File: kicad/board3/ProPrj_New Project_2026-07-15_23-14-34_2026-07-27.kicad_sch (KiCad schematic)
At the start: 141 parts, among them P1 WJ500V-5.08-2P, P2 WJ500V-5.08-2P, Q1 AO4406A, Q2 AO4406A, SW1 HX TS4538CJ 250gf 009, SW2 HX TS4538CJ 250gf 009, SW3 HX TS4538CJ 250gf 009, SW4 HX TS4538CJ 250gf 009, SW6 HX TS4538CJ 250gf 009, SW7 HX TS4538CJ 250gf 009, U1 STM32H755ZIT6, U10 TBD62083AFWG, U2 W25Q512JVEIQ TR, U3 TPS563201DDCR, U4 CH224K, U5 LM74700QDBVRQ1, U6 LM74700QDBVRQ1, U7 FM24CL64B-GTR, U8 TJA1051T/3/1J, U9 TJA1051T/3/1J, X1 25MHz

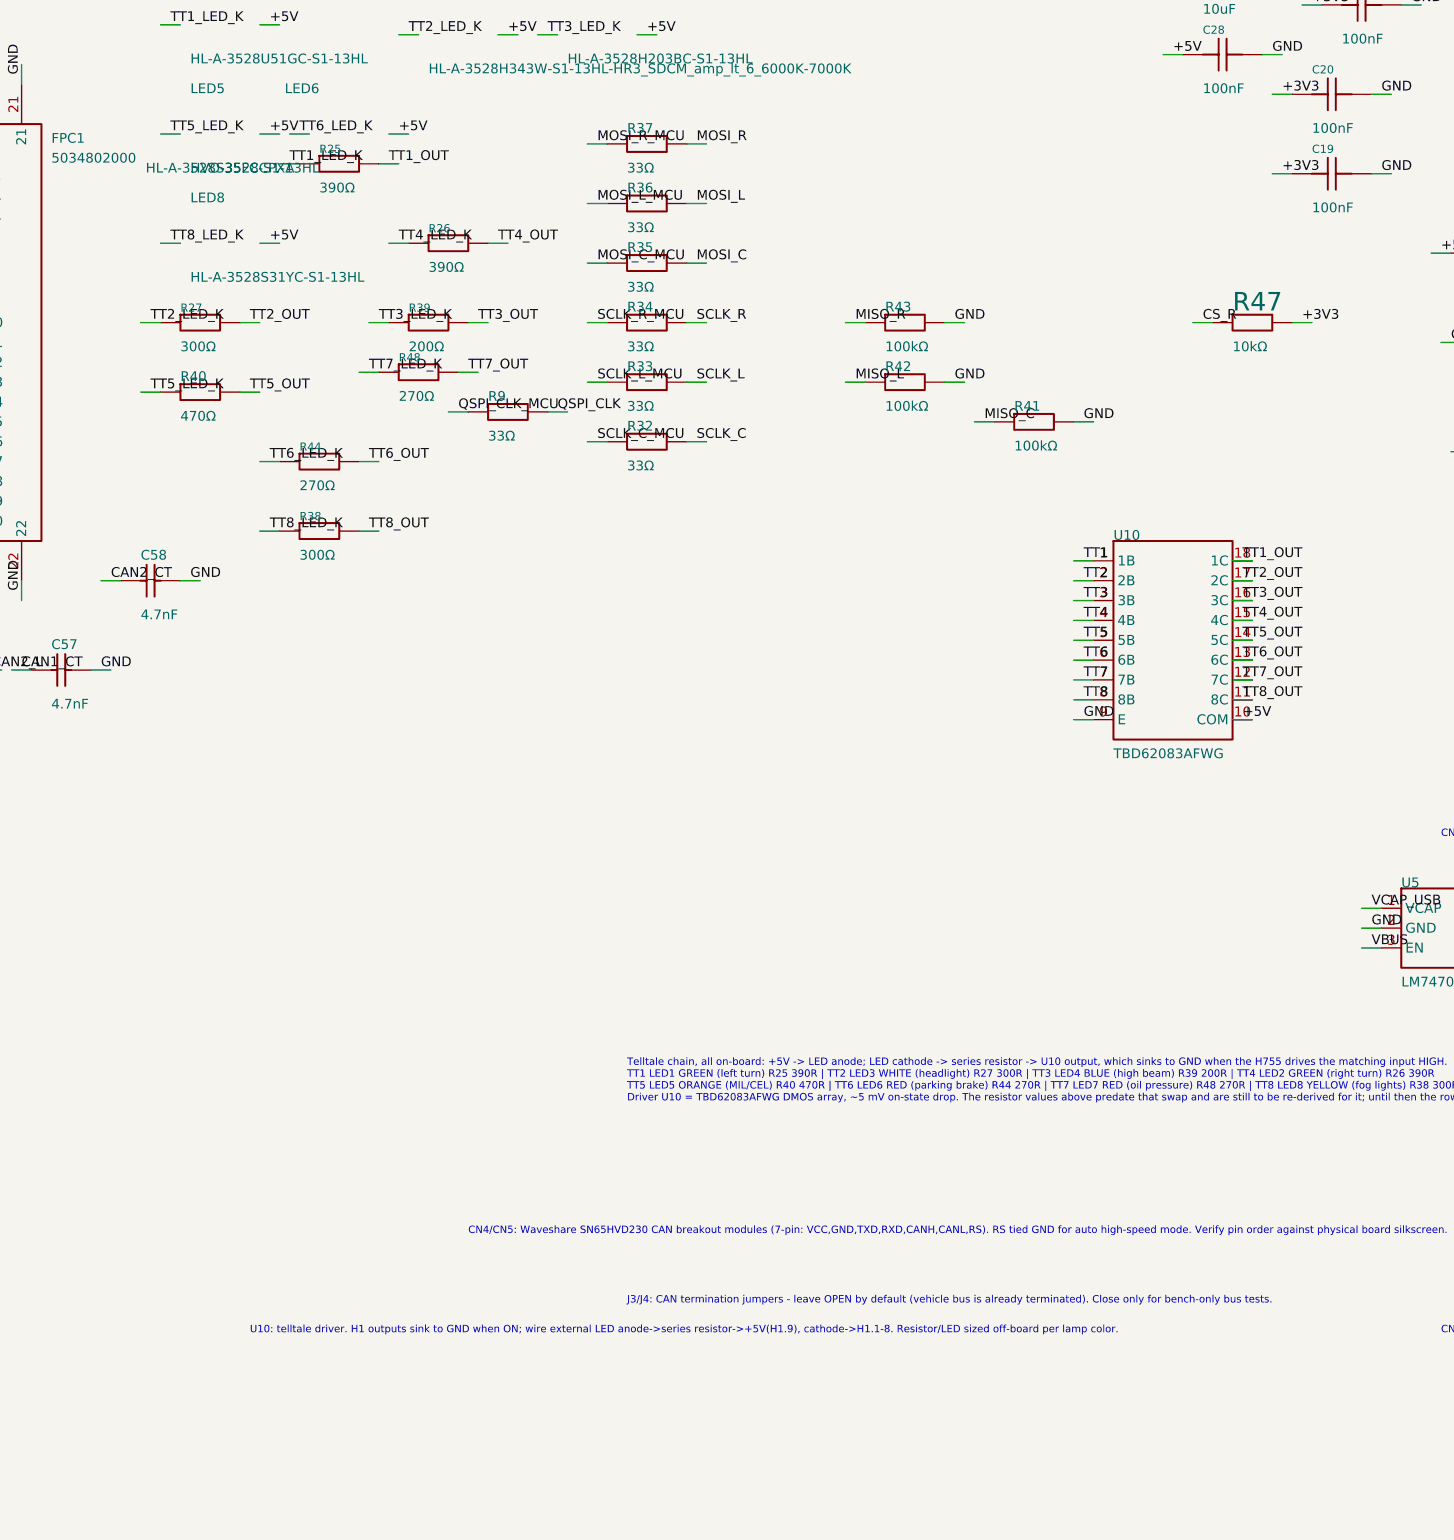
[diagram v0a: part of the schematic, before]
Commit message: feat(kicad): U19 - schematic moves telltale drive onto two AW9523B expanders
Datasheet gate PASSED before any wiring (AW9523B V2.4, official Awinic PDF):
IMAX 31.9/37/43.1 mA with 256 linear steps (10-20 mA targets sit mid-range;
GCR ISEL can halve the range for double resolution); all pins rated -0.3..6 V
independent of VCC; I2C thresholds FIXED at VIH 1.4 V / VIL 0.4 V, so the
3.3 V-pulled trunk works at any VCC; POR defaults are GPIO *output* with the
state set by the AD straps - GND/GND would light every LED at power-up.

Decisions locked by the gate: VCC = +5 V both ICs (POR high equals the
anode rail, LEDs hard off; 3.3 V would leave ~1.7 V across red/yellow).
West U11 = AD1/AD0 both +5V -> 0x5B, every port POR-safe. East U12 =
AD1 +5V / AD0 GND -> 0x5A, LEDs on its POR-safe P1_4-P1_7 (west matches for
firmware symmetry). RSTN tied to +5V (internal 100k pull-DOWN would hold the
chip in reset). INTN + 24 spare I/O carry no_connects.

Schematic: U10 (TBD62083) and R25-R27/R38-R40/R44/R48 deleted with their
TT/TT_OUT labels and wires; C61/C62 100nF (C14663) decouple the new ICs.
Netlist diff is exactly the intended topology: 16 TT nets gone, each
TTn_LED_K keeps its LED and gains its expander pin, I2C gains two loads,
BTN nets byte-identical (KTD20/R40 proof). ERC 171 -> 155 (pin_not_driven
71 -> 55), no new types. All surviving instances verified byte-identical.

Board deliberately NOT yet synced - not fab-ready at this boundary. Next:
Kevin runs Update PCB from Schematic (KiCad restarted, re-link by reference)
per KTD12, then U20 places and routes.

Known pre-existing, not introduced here: kicad_lcsc duplicates flags 10k
R0603 dual-sourced (C25804 x4 / C98220 x6) on parts this change never touched.

Co-Authored-By: Claude Fable 5 <noreply@anthropic.com>
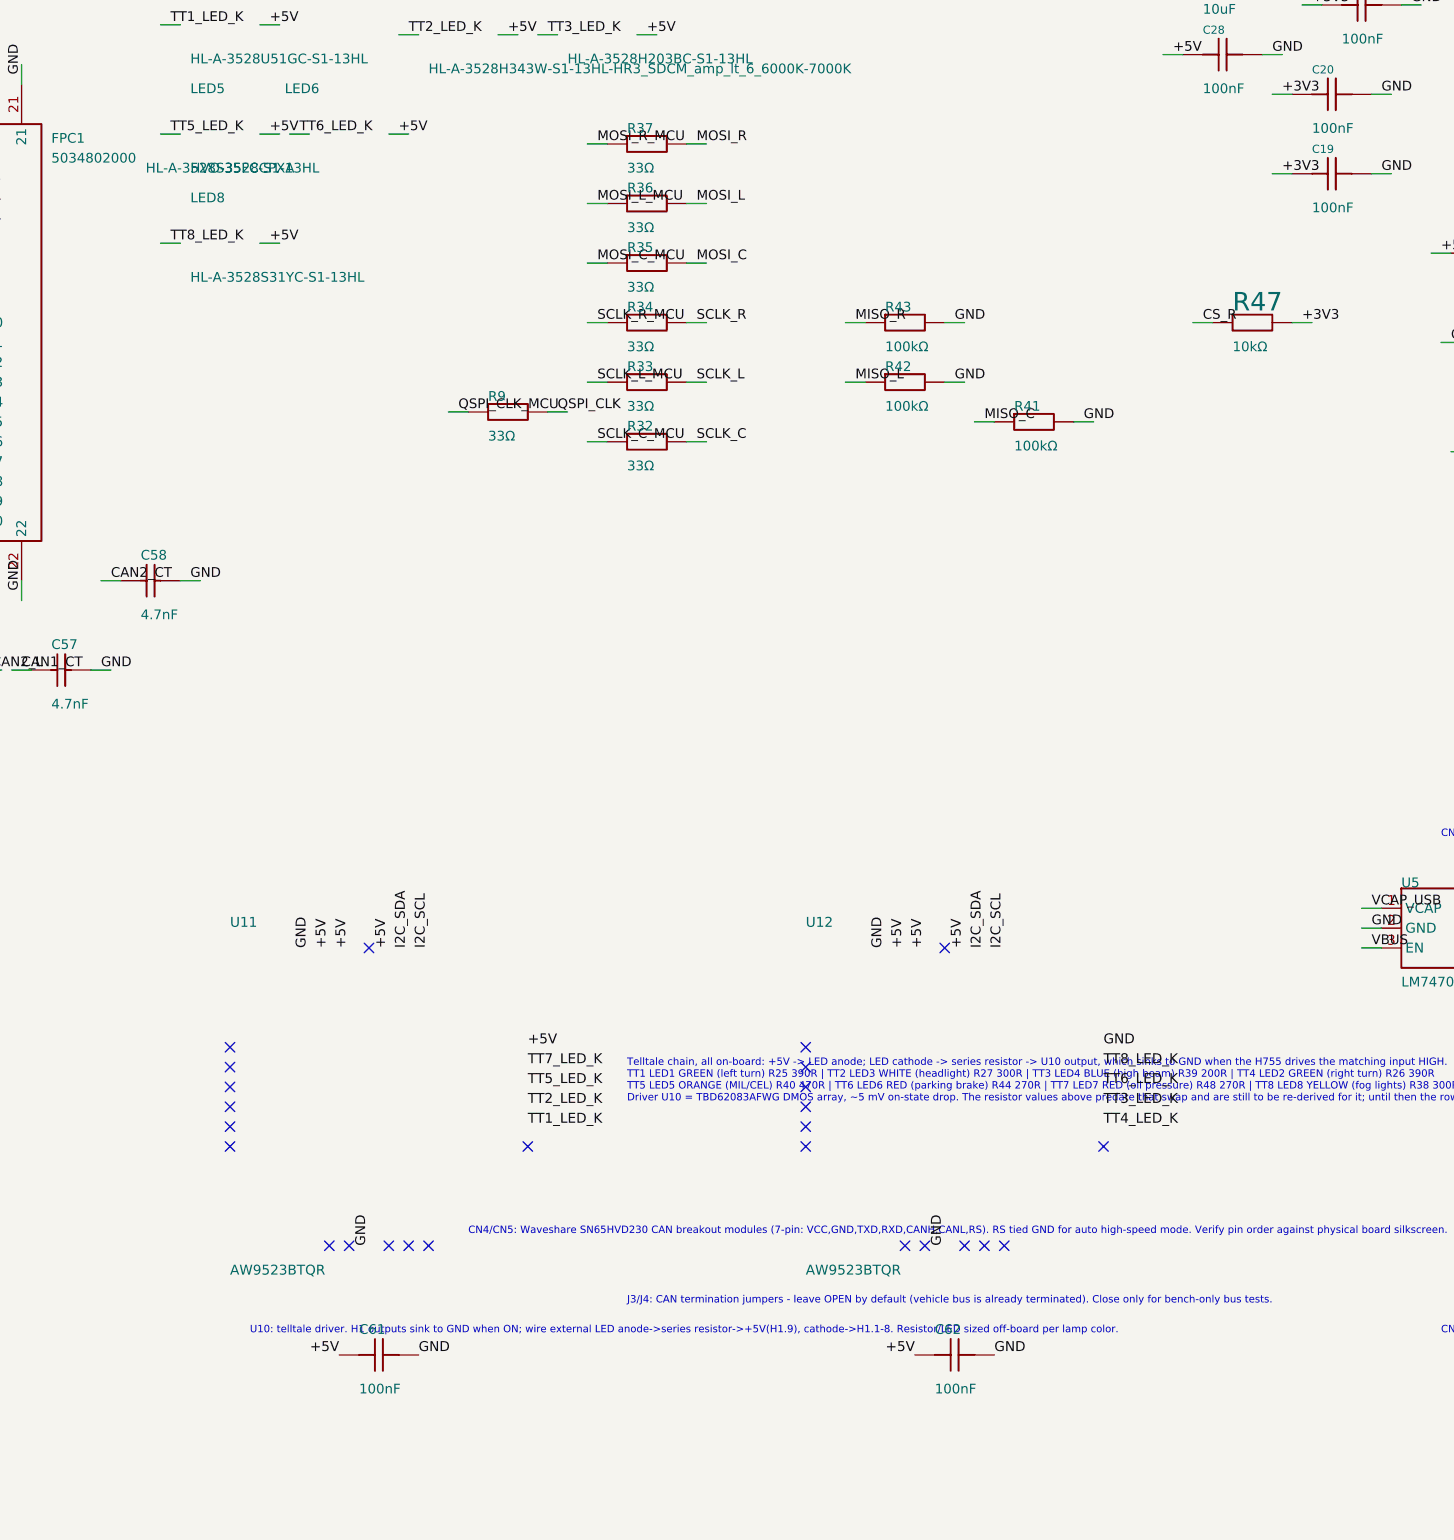
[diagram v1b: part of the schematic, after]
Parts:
- removed R25, R26: 390Ω, ProPrj_New-easyedapro:R0603, symbol ProPrj_New-easyedapro:0603WAF3900T5E
- removed R27, R38: 300Ω, ProPrj_New-easyedapro:R0603, symbol ProPrj_New-easyedapro:0603WAF3000T5E
- removed R39: 200Ω, ProPrj_New-easyedapro:R0603, symbol ProPrj_New-easyedapro:0603WAF2000T5E
- removed R40: 470Ω, ProPrj_New-easyedapro:R0603, symbol ProPrj_New-easyedapro:0603WAF4700T5E
- removed R44, R48: 270Ω, ProPrj_New-easyedapro:R0603, symbol ProPrj_New-easyedapro:0603WAF2700T5E
- removed U10: TBD62083AFWG, ProPrj_New-easyedapro:SOIC-18_L11.6-W7.5-P1.27-LS10.3-BL, symbol ProPrj_New-easyedapro:TBD62083AFWG_C165895
- added C61, C62: 100nF, ProPrj_New-easyedapro:C0603, symbol ProPrj_New-easyedapro:CC0603KRX7R9BB104
- added U11, U12: AW9523BTQR, JLCImport:AW9523BTQR, symbol JLCImport:AW9523BTQR
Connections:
- net +5V: now also C61.1, C62.1, U11.18 (AD0), U11.21 (VCC), U11.23 (RSTN), U11.24 (AD1), U12.21 (VCC), U12.23 (RSTN), U12.24 (AD1)
- net GND: now also C61.2, C62.2, U11.25 (GND), U11.9 (GND), U12.18 (AD0), U12.25 (GND), U12.9 (GND)
- net I2C_SCL: now also U11.19 (SCL), U12.19 (SCL)
- net I2C_SDA: now also U11.20 (SDA), U12.20 (SDA)
- net TT1_LED_K: now also U11.14 (P1_4)
- net TT2_LED_K: now also U11.15 (P1_5)
- net TT3_LED_K: now also U12.15 (P1_5)
- net TT4_LED_K: now also U12.14 (P1_4)
- net TT5_LED_K: now also U11.16 (P1_6)
- net TT6_LED_K: now also U12.16 (P1_6)
- net TT7_LED_K: now also U11.17 (P1_7)
- net TT8_LED_K: now also U12.17 (P1_7)
- no-connect marks 9 -> 35

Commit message: feat(kicad): U13 done + U14 partial -- SMD bulk conversion, 4/6 caps placed
U13 (schematic, netlist-verified): the six 220uF THT electrolytics are
deleted; the per-FPC 10uF becomes 22uF (C45783, JLC Basic, properties
swapped in place); six new caps added per the manufacturer's decoupling
spec -- 100nF at each FPC's BLVDD (C63-65) and 10uF at each FPC's 3V3
(C66-68). Each FPC already carried a 3V3 100nF (C17/18/19), so no
additions there. Total +5V bulk drops 880uF -> 66uF at the loads.

U14 (board, WIP): C63, C64, C65, C68 placed and stub-connected by a
collision-searching placer -- kicad_verify NEW=0, violations 35 < 36
baseline (one starved thermal resolved). Outstanding: C66 (FPC1) and
C67 (FPC2) have no legal pocket in the searched envelopes (south
fields are walled by VBUS_SENSE, the SCLK In2 river, and TT2's B-layer
run); 5 airwires pending until they are placed and connected. Fab
regen deferred until the board closes.

Co-Authored-By: Claude Fable 5 <noreply@anthropic.com>
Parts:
- removed C1, C12, C13, C14, C16, C2: ERS1EM221F12OT, ProPrj_New-easyedapro:CAP-TH_BD8.0-P3.50-D0.6-FD, symbol ProPrj_New-easyedapro:CAPACITOR_THT{colon}CP_RADIAL_D8.0MM_P2.50MM
- added C63, C64, C65: 100nF, ProPrj_New-easyedapro:C0603, symbol ProPrj_New-easyedapro:CC0603KRX7R9BB104
- added C66, C67, C68: 22uF, ProPrj_New-easyedapro:C0805, symbol ProPrj_New-easyedapro:CL21A106KAYNNNE
- C29, C30, C31: value 10uF -> 22uF; LCSC Part Name 10uF ±10% 25V -> 22uF ±20% 25V; Manufacturer SAMSUNG(三星) -> SAMSUNG; Manufacturer Part CL21A106KAYNNNE -> CL21A226MAQNNNE; Supplier Part C15850 -> C45783
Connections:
- net +3V3: now also C66.1, C67.1, C68.1
- net +5V: now also C63.1, C64.1, C65.1
- net GND: now also C63.2, C64.2, C65.2, C66.2, C67.2, C68.2

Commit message: fix(kicad): C67 out of FPC2's FFC insertion path
Kevin caught it on review: C67 sat 0.32 mm from FPC2's north face --
directly in the flat-flex ribbon's approach, which DRC cannot see.
Relocated to the west pocket at (140.35, 92.70) as a 0603 10uF
(C19702, JLC Basic; ~8uF effective at 3.3V, inside the 4.7-10uF spec)
since the 0805 fits no south pocket. Standing rule for this board: the
strip between each FPC's north face and the board edge is cable
territory -- no components. Gates unchanged: NEW=0, 35 violations,
airwires the 5 diagnosed legacy items.

Co-Authored-By: Claude Fable 5 <noreply@anthropic.com>
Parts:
- C67: footprint ProPrj_New-easyedapro:C0805 -> ProPrj_New-easyedapro:C0603; LCSC Part Name 22uF ±20% 25V -> 10uF ±10% 10V; Manufacturer Part CL21A226MAQNNNE -> CL10A106KP8NNNC; Supplier Part C45783 -> C19702
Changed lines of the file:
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@@
 			)
 		)
-		(property "Footprint" "ProPrj_New-easyedapro:C0805"
+		(property "Footprint" "ProPrj_New-easyedapro:C0603"
 			(at 132.08 287.02 0)
 			(hide yes)
@@
 			)
 		)
-		(property "Datasheet" "https://item.szlcsc.com/datasheet/CL21A226MAQNNNE/45783.html"
+		(property "Datasheet" "https://item.szlcsc.com/datasheet/CL10A106KP8NNNC/19702.html"
 			(at 132.08 287.02 0)
 			(hide yes)
@@
 			)
 		)
-		(property "Manufacturer Part" "CL21A226MAQNNNE"
+		(property "Manufacturer Part" "CL10A106KP8NNNC"
 			(at 132.08 287.02 0)
 			(hide yes)
@@
 			)
 		)
-		(property "Supplier Part" "C45783"
+		(property "Supplier Part" "C19702"
 			(at 132.08 287.02 0)
 			(hide yes)
@@
 			)
 		)
-		(property "LCSC Part Name" "22uF ±20% 25V"
+		(property "LCSC Part Name" "10uF ±10% 10V"
 			(at 132.08 287.02 0)
 			(hide yes)

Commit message: fix(kicad): re-source U2 to W25Q256JVEIQ -- 4 units of stock to 23,508
U24 of the pre-fab plan. The review flagged U2 at 4 units of JLCPCB stock
on a required single-instance part and asked for a pin-compatible
alternative. Live re-verification showed that recommendation cannot be
satisfied as written: at 512 Mbit, C7389628 is 4, C2986165 is 3, and every
other variant is 0 or a different package. The only healthy-stock 512 Mbit
is SOIC-16, which is a footprint change and a full GUI sync.

One capacity step down solves it on the identical land pattern. C97522
(W25Q256JVEIQ, WSON-8-EP 6x8) holds 23,508 units at $4.63 -- cheaper than
the part it replaces -- with C2682312 at 1,331 as a second source.

Pinout verified pin-for-pin before the swap rather than assumed from
Winbond series convention: all 9 pins including the exposed pad match,
differing only in notation (/CS vs CS#).

Capacity is not a constraint. The 2026-07-24 carrier plan records the
external NOR's purpose as "asset headroom" for a ~1.81 MB firmware image;
the splash pack is ~1.66 MB and fonts ~324 KB against 32 MB. That plan also
notes the production board upgrades this NOR to AEC-Q100 anyway.

Worth noting how fast this moved: the same plan's sourcing snapshot
recorded 2,163 units on 2026-07-24. It was 4 seven days later.

Land pattern, position, rotation and every pad-to-net assignment are
unchanged, so no GUI sync is needed for this unit. Updated on both sides
plus the library footprint's default Value, and in the descriptive
LCSC Part Name field which still claimed 512Mbit.

Known residual: the library symbol is still *named* "W25Q512JVEIQ TR" in
its lib_id. That identifier reaches no fabricated output -- the BOM reads
Supplier Part and the marking layer reads Value, both now correct -- and
renaming it means editing a 26k-line symbol library plus every cached
reference. Better done during the coming GUI sync pass.

U1 (STM32H755ZIT6, C730212) re-checked in the same pass: still 37 units,
and its only 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
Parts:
- U2: value W25Q512JVEIQ TR -> W25Q256JVEIQ; LCSC Part Name 支持双/四SPI接口的3V、512Mbit 串行闪存 -> 支持双/四SPI接口的3V、256Mbit 串行闪存; Manufacturer Part W25Q512JVEIQ TR -> W25Q256JVEIQ; Supplier Part C7389628 -> C97522
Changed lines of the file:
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@@
 			)
 		)
-		(property "Value" "W25Q512JVEIQ TR"
+		(property "Value" "W25Q256JVEIQ"
 			(at 86.36 92.71 0)
 			(show_name no)
@@
 			)
 		)
-		(property "Datasheet" "https://item.szlcsc.com/datasheet/W25Q512JVEIQ%2520TR/8361477.html"
+		(property "Datasheet" "https://item.szlcsc.com/datasheet/W25Q256JVEIQ/1811142.html"
 			(at 110.49 81.28 0)
 			(hide yes)
@@
 			)
 		)
-		(property "Manufacturer Part" "W25Q512JVEIQ TR"
+		(property "Manufacturer Part" "W25Q256JVEIQ"
 			(at 110.49 81.28 0)
 			(hide yes)
@@
 			)
 		)
-		(property "Supplier Part" "C7389628"
+		(property "Supplier Part" "C97522"
 			(at 110.49 81.28 0)
 			(hide yes)
@@
 			)
 		)
-		(property "LCSC Part Name" "支持双/四SPI接口的3V、512Mbit 串行闪存"
+		(property "LCSC Part Name" "支持双/四SPI接口的3V、256Mbit 串行闪存"
 			(at 110.49 81.28 0)
 			(hide yes)

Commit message: fix(kicad): RSTN reset networks on U11/U12 and a PTC on the barrel input
U25, closing the review's CRITICAL and the protection HIGH.

RSTN (CRITICAL). Both AW9523B expanders had pin 23 hard-tied to /+5V,
violating the datasheet's mandatory ~100us RSTN-low-after-VCC sequence --
and that POR logic is the telltales' only passive protection since KTD17
removed the series resistors and the DMOS driver. Each IC now gets 10k +
100nF with a 1N5819WS Schottky across the resistor, cathode to +5V. The
diode is the part that matters: a plain RC holds charge through a fast
brownout, so RSTN never goes low and the fix silently fails in exactly the
vehicle-rail scenario the finding was raised for.

PTC (HIGH). No fuse or PTC existed anywhere on the board. F1
(BSMD1812-200-30V, 2A hold / 4A trip, ~20mOhm, Basic library) now sits
between DC1 and the Q2/U6 ideal-diode path.

Inserting it in series took two edits, not one. Adding F1 with a DC1_IN
label left /DC1_IN holding only F1 pin 1 -- a dangling stub, with DC1 and
F1 pin 2 still sharing /+5V_BARREL, so the PTC was bridged rather than in
series. Retargeting DC1's own pin label was the second half. Netlist proves
the final topology: /DC1_IN = DC1.1 + F1.1, /+5V_BARREL = F1.2 + Q2 + U6 +
C54, with DC1 no longer on it.

Connectivity is by label throughout, which is how this schematic already
works (490 labels, zero global/hierarchical) and how pin 23 was tied to
+5V in the first place -- a bare label on the pin, no wire. That made the
break a rename and avoided the whole class of "wire stub misses the pin by
one grid step".

Also in this pass: C67's Value corrected 22uF -> 10uF to match its sourced
C19702 and the board footprint; the U10/TBD62083 telltale-chain text, the
R25-R48 resistor table and the CN4/CN5 SN65HVD230 breakout note deleted as
superseded architecture; the "5V/15A" supply note rewritten to name F1 and
flag the supply rating as unconfirmed rather than asserting it.

Verified: 136 -> 143 components, 225 -> 228 nets (ex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
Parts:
- added C70, C71: 100nF, ProPrj_New-easyedapro:C0603, symbol ProPrj_New-easyedapro:CC0603KRX7R9BB104
- added D10, D11: 1N5819WS, JLCImport:1N5819WS, symbol JLCImport:1N5819WS
- added F1: BSMD1812-200-30V, JLCImport:BSMD1812-200-30V, symbol JLCImport:BSMD1812-200-30V
- added R60, R61: 10kΩ, ProPrj_New-easyedapro:R0603, symbol ProPrj_New-easyedapro:0603WAF1002T5E
- C67: value 22uF -> 10uF
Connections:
- net +5V: now also D10.2 (A), D11.2 (A), R60.1, R61.1; no longer U11.23 (RSTN), U12.23 (RSTN)
- net +5V_BARREL: now also F1.2; no longer DC1.1
- net GND: now also C70.2, C71.2
- new net DC1_IN: DC1.1, F1.1
- new net U11_RSTN: C70.1, D10.1 (K), R60.2, U11.23 (RSTN)
- new net U12_RSTN: C71.1, D11.1 (K), R61.2, U12.23 (RSTN)
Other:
- note added: "J1/DC1: +5V IN via F1 PPTC (2A hold / 4A trip). Supply rating UNCONFIRMED -- the old "5V/15A" note was stale; confirm before relying on it."
- note removed: "CN4/CN5: Waveshare SN65HVD230 CAN breakout modules (7-pin: VCC,GND,TXD,RXD,CANH,CANL,RS). RS tied GND for auto high-speed mode. Verify pin order against physical board silkscreen."
- note removed: "J1: +5V IN (dedicated 5V/15A supply)"
- note removed: "Telltale chain, all on-board: +5V -> LED anode; LED cathode -> series resistor -> U10 output, which sinks to GND when the H755 drives the matching input HIGH. TT1 LED1 GREEN (left turn) R25 390R | TT2 LED3 WHITE (headlight) R27 300R | TT3 LED4 BLUE (high beam) R39 200R | TT4 LED2 GREEN (right turn) R26 390R TT5 LED5 ORANGE (MIL/CEL) R40 470R | TT6 LED6 RED (parking brake) R44 270R | TT7 LED7 RED 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"
- note removed: "U10: telltale driver. H1 outputs sink to GND when ON; wire external LED anode->series resistor->+5V(H1.9), cathode->H1.1-8. Resistor/LED sized off-board per lamp color."
